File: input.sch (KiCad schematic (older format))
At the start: 12 parts

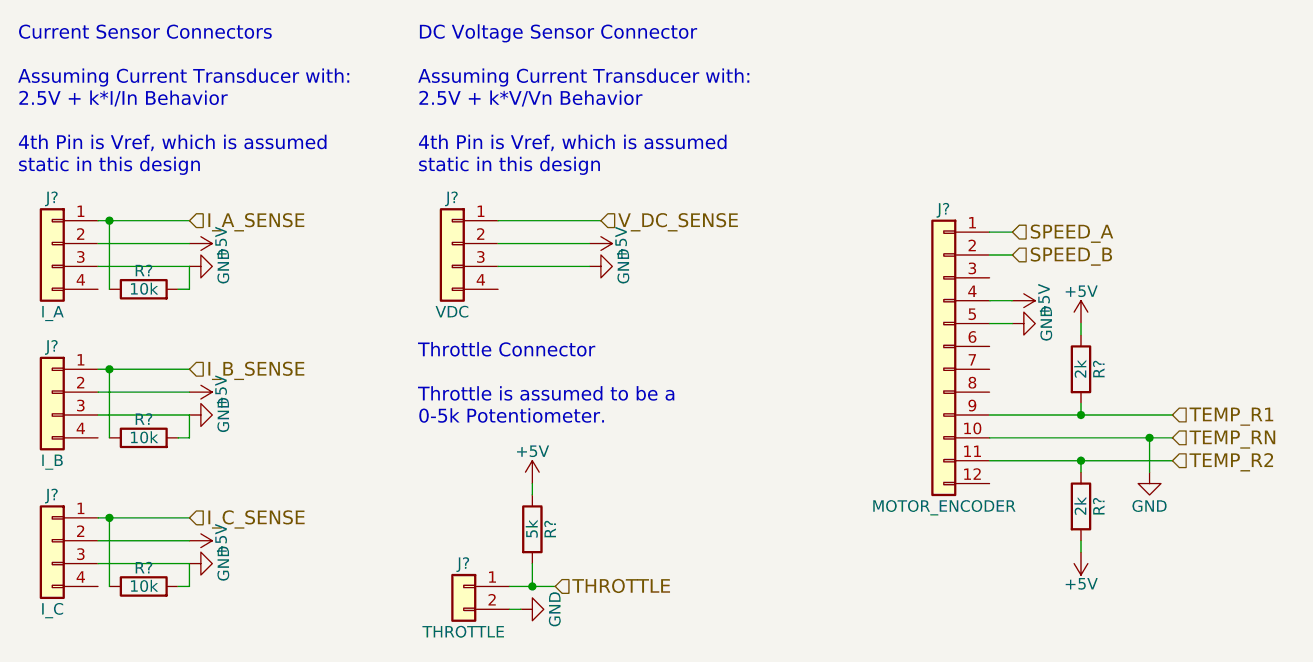
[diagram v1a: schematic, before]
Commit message: Break up input into separate schematics.
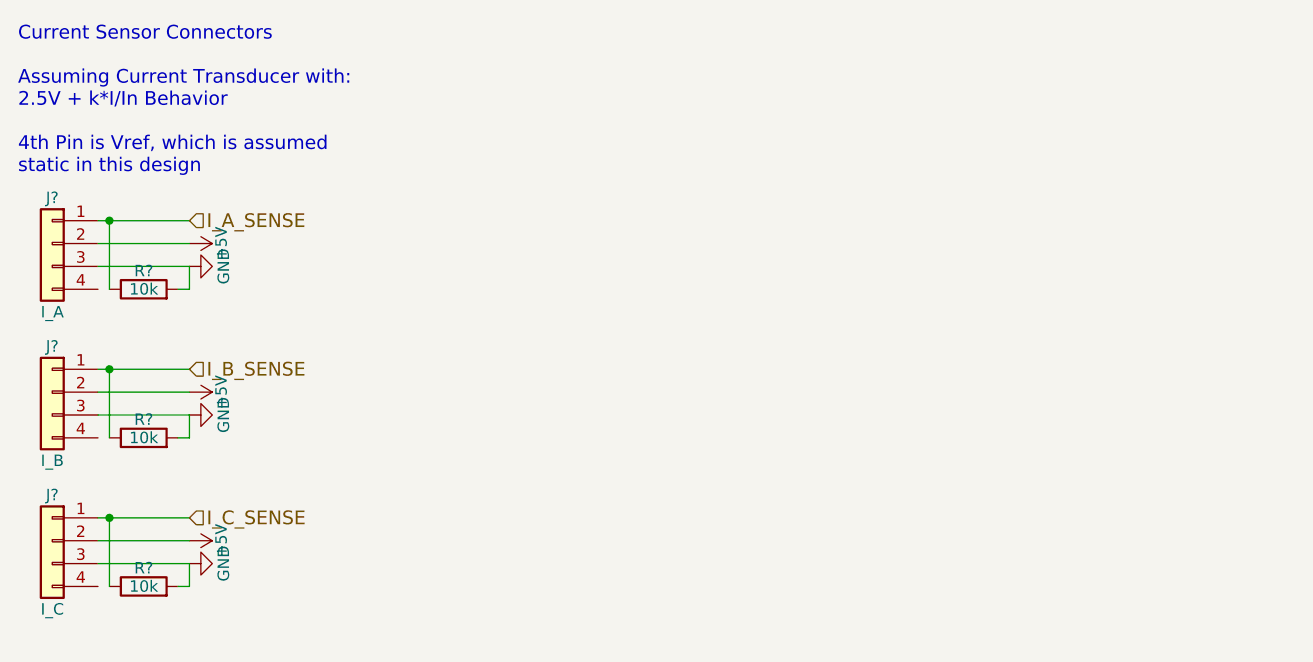
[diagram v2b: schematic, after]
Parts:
- removed J?: THROTTLE, symbol Conn_01x02
- removed J?: MOTOR_ENCODER, symbol Conn_01x12
- removed J?: VDC, symbol Conn_01x04
- removed R?: 5k, symbol R
- removed R? (x2): 2k, symbol R
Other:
- note removed: "DC Voltage Sensor Connector\n\nAssuming Current Transducer with:\n2.5V + k*V/Vn Behavior\n\n4th Pin is Vref, which is assumed\nstatic in this design"
- note removed: "Throttle Connector\n\nThrottle is assumed to be a \n0-5k Potentiometer."
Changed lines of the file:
@@
 $Descr A4 11693 8268
 encoding utf-8
-Sheet 3 6
+Sheet 7 9
 Title ""
 Date ""
@@
 	0    -1   -1   0
 $EndComp
-$Comp
-L GND #PWR?
-U 1 1 5AEC7A09
-P 4200 2300
-F 0 "#PWR?" H 4200 2050 50  0001 C CNN
-F 1 "GND" H 4200 2150 50  0000 C CNN
-F 2 "" H 4200 2300 50  0001 C CNN
-F 3 "" H 4200 2300 50  0001 C CNN
-	1    4200 2300
-	0    -1   -1   0
-$EndComp
-$Comp
-L Conn_01x02 J?
-U 1 1 5AEC7A10
-P 3650 3700
-F 0 "J?" H 3650 3800 50  0000 C CNN
-F 1 "THROTTLE" H 3650 3500 50  0000 C CNN
-F 2 "" H 3650 3700 50  0001 C CNN
-F 3 "" H 3650 3700 50  0001 C CNN
-	1    3650 3700
-	-1   0    0    -1
-$EndComp
-$Comp
-L GND #PWR?
-U 1 1 5AEC7A17
-P 3900 3800
-F 0 "#PWR?" H 3900 3550 50  0001 C CNN
-F 1 "GND" H 3900 3650 50  0000 C CNN
-F 2 "" H 3900 3800 50  0001 C CNN
-F 3 "" H 3900 3800 50  0001 C CNN
-	1    3900 3800
-	0    -1   -1   0
-$EndComp
-$Comp
-L R R?
-U 1 1 5AEC7A1E
-P 3950 3450
-F 0 "R?" V 4030 3450 50  0000 C CNN
-F 1 "5k" V 3950 3450 50  0000 C CNN
-F 2 "" V 3880 3450 50  0001 C CNN
-F 3 "" H 3950 3450 50  0001 C CNN
-	1    3950 3450
-	1    0    0    -1
-$EndComp
-$Comp
-L +5V #PWR?
-U 1 1 5AEC7A25
-P 3950 3250
-F 0 "#PWR?" H 3950 3100 50  0001 C CNN
-F 1 "+5V" H 3950 3390 50  0000 C CNN
-F 2 "" H 3950 3250 50  0001 C CNN
-F 3 "" H 3950 3250 50  0001 C CNN
-	1    3950 3250
-	1    0    0    -1
-$EndComp
-$Comp
-L Conn_01x12 J?
-U 1 1 5AEC7A2B
-P 5750 2650
-F 0 "J?" H 5750 3250 50  0000 C CNN
-F 1 "MOTOR_ENCODER" H 5750 1950 50  0000 C CNN
-F 2 "" H 5750 2650 50  0001 C CNN
-F 3 "" H 5750 2650 50  0001 C CNN
-	1    5750 2650
-	-1   0    0    -1
-$EndComp
-$Comp
-L +5V #PWR?
-U 1 1 5AEC7A32
-P 6050 2450
-F 0 "#PWR?" H 6050 2300 50  0001 C CNN
-F 1 "+5V" H 6050 2590 50  0000 C CNN
-F 2 "" H 6050 2450 50  0001 C CNN
-F 3 "" H 6050 2450 50  0001 C CNN
-	1    6050 2450
-	0    1    1    0
-$EndComp
-$Comp
-L GND #PWR?
-U 1 1 5AEC7A38
-P 6050 2550
-F 0 "#PWR?" H 6050 2300 50  0001 C CNN
-F 1 "GND" H 6050 2400 50  0000 C CNN
-F 2 "" H 6050 2550 50  0001 C CNN
-F 3 "" H 6050 2550 50  0001 C CNN
-	1    6050 2550
-	0    -1   -1   0
-$EndComp
-$Comp
-L R R?
-U 1 1 5AEC7A43
-P 6350 2750
-F 0 "R?" V 6430 2750 50  0000 C CNN
-F 1 "2k" V 6350 2750 50  0000 C CNN
-F 2 "" V 6280 2750 50  0001 C CNN
-F 3 "" H 6350 2750 50  0001 C CNN
-	1    6350 2750
-	1    0    0    -1
-$EndComp
-$Comp
-L R R?
-U 1 1 5AEC7A4A
-P 6350 3350
-F 0 "R?" V 6430 3350 50  0000 C CNN
-F 1 "2k" V 6350 3350 50  0000 C CNN
-F 2 "" V 6280 3350 50  0001 C CNN
-F 3 "" H 6350 3350 50  0001 C CNN
-	1    6350 3350
-	1    0    0    -1
-$EndComp
-$Comp
-L GND #PWR?
-U 1 1 5AEC7A51
-P 6650 3200
-F 0 "#PWR?" H 6650 2950 50  0001 C CNN
-F 1 "GND" H 6650 3050 50  0000 C CNN
-F 2 "" H 6650 3200 50  0001 C CNN
-F 3 "" H 6650 3200 50  0001 C CNN
-	1    6650 3200
-	1    0    0    -1
-$EndComp
-$Comp
-L +5V #PWR?
-U 1 1 5AEC7A57
-P 6350 2550
-F 0 "#PWR?" H 6350 2400 50  0001 C CNN
-F 1 "+5V" H 6350 2690 50  0000 C CNN
-F 2 "" H 6350 2550 50  0001 C CNN
-F 3 "" H 6350 2550 50  0001 C CNN
-	1    6350 2550
-	1    0    0    -1
-$EndComp
-$Comp
-L +5V #PWR?
-U 1 1 5AEC7A5D
-P 6350 3550
-F 0 "#PWR?" H 6350 3400 50  0001 C CNN
-F 1 "+5V" H 6350 3690 50  0000 C CNN
-F 2 "" H 6350 3550 50  0001 C CNN
-F 3 "" H 6350 3550 50  0001 C CNN
-	1    6350 3550
-	-1   0    0    1
-$EndComp
 Wire Wire Line
 	2450 2300 2050 2300
@@
 Wire Wire Line
 	2450 3700 2450 3600
-Wire Wire Line
-	3900 3800 3850 3800
-Wire Wire Line
-	3850 3700 4050 3700
-Wire Wire Line
-	3950 3600 3950 3700
-Connection ~ 3950 3700
-Wire Wire Line
-	3950 3300 3950 3250
-Wire Wire Line
-	5950 2950 6750 2950
-Wire Wire Line
-	5950 3050 6750 3050
-Wire Wire Line
-	5950 3150 6750 3150
-Wire Wire Line
-	6050 2550 5950 2550
-Wire Wire Line
-	6050 2450 5950 2450
-Wire Wire Line
-	6050 2250 5950 2250
-Wire Wire Line
-	6050 2150 5950 2150
-Wire Wire Line
-	6650 3050 6650 3200
-Wire Wire Line
-	6350 3200 6350 3150
-Connection ~ 6350 3150
-Wire Wire Line
-	6350 2900 6350 2950
-Connection ~ 6350 2950
-Wire Wire Line
-	6350 2550 6350 2600
-Wire Wire Line
-	6350 3500 6350 3550
 $Comp
 L Conn_01x04 J?
@@
 	2100 3700 2100 3400
 Connection ~ 2100 3400
-Text Notes 3450 1900 0    60   ~ 0
-DC Voltage Sensor Connector\n\nAssuming Current Transducer with:\n2.5V + k*V/Vn Behavior\n\n4th Pin is Vref, which is assumed\nstatic in this design
-Text Notes 3450 3000 0    60   ~ 0
-Throttle Connector\n\nThrottle is assumed to be a \n0-5k Potentiometer.
-$Comp
-L Conn_01x04 J?
-U 1 1 5AEC7AA9
-P 3600 2200
-F 0 "J?" H 3600 2400 50  0000 C CNN
-F 1 "VDC" H 3600 1900 50  0000 C CNN
-F 2 "" H 3600 2200 50  0001 C CNN
-F 3 "" H 3600 2200 50  0001 C CNN
-	1    3600 2200
-	-1   0    0    -1
-$EndComp
-$Comp
-L +5V #PWR?
-U 1 1 5AEC7AB0
-P 4200 2200
-F 0 "#PWR?" H 4200 2050 50  0001 C CNN
-F 1 "+5V" H 4200 2340 50  0000 C CNN
-F 2 "" H 4200 2200 50  0001 C CNN
-F 3 "" H 4200 2200 50  0001 C CNN
-	1    4200 2200
-	0    1    1    0
-$EndComp
-Wire Wire Line
-	4250 2100 3800 2100
-Wire Wire Line
-	4200 2200 3800 2200
-Wire Wire Line
-	4200 2300 3800 2300
 Text HLabel 2450 2100 2    60   Input ~ 0
 I_A_SENSE
@@
 Text HLabel 2450 3400 2    60   Input ~ 0
 I_C_SENSE
-Text HLabel 4250 2100 2    60   Input ~ 0
-V_DC_SENSE
-Text HLabel 4050 3700 2    60   Input ~ 0
-THROTTLE
-Text HLabel 6050 2150 2    60   Input ~ 0
-SPEED_A
-Text HLabel 6050 2250 2    60   Input ~ 0
-SPEED_B
-Text HLabel 6750 2950 2    60   Input ~ 0
-TEMP_R1
-Text HLabel 6750 3150 2    60   Input ~ 0
-TEMP_R2
-Text HLabel 6750 3050 2    60   Input ~ 0
-TEMP_RN
-Connection ~ 6650 3050
 $EndSCHEMATC
